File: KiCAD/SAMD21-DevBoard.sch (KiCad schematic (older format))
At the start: 23 parts, among them J1 .1\" Headers, J2 .1\" Headers, J3 Cortex_Debug, SW1 FSMCTTR, U1 SAMD21G18A-AU, Y1 32.768KHz

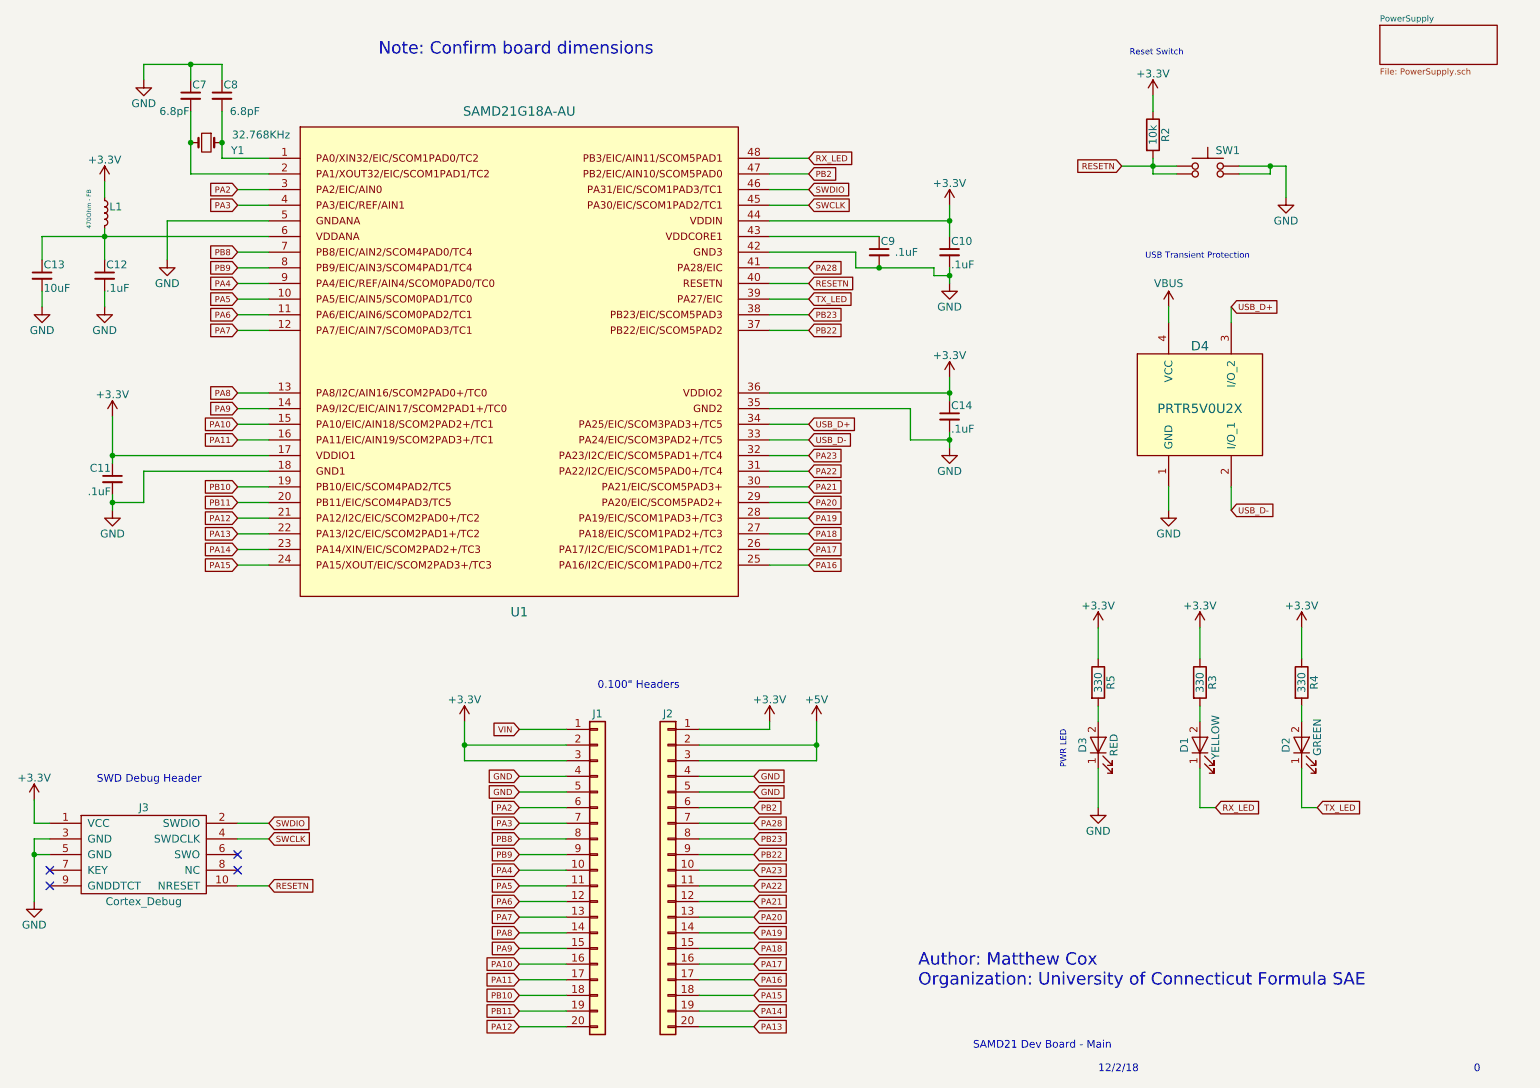
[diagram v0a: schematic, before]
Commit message: Fix library error
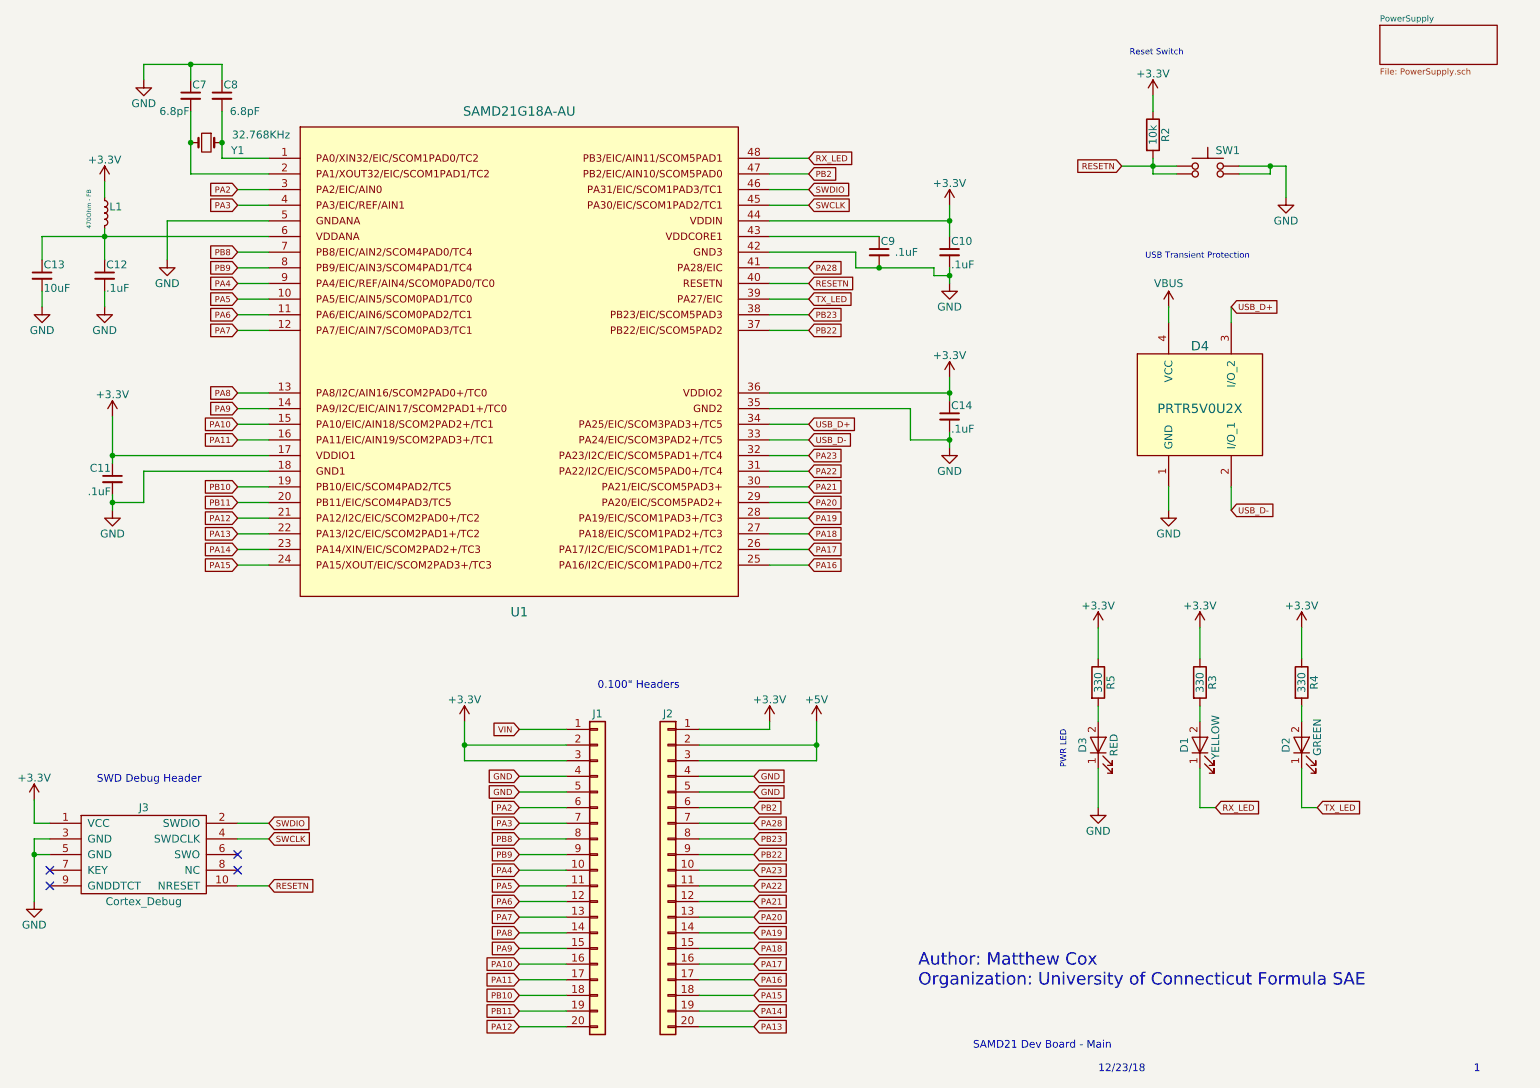
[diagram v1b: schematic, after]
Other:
- note added: "12/23/18"
- note added: "1\n"
- note removed: "0"
- note removed: "12/2/18"
- note removed: "Note: Confirm board dimensions"
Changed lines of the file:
@@
 EESchema Schematic File Version 2
+LIBS:SAMD21-DevBoard-rescue
 LIBS:power
 LIBS:device
@@
 SAMD21 Dev Board - Main
 Text Notes 8200 7650 0    49   ~ 0
-12/2/18
+12/23/18
 Text Notes 10600 7650 0    49   ~ 0
-0
+1\n
 Text Notes 7050 7100 0    79   ~ 0
 Author: Matthew Cox\nOrganization: University of Connecticut Formula SAE
@@
 	1    0    0    -1
 $EndComp
-Text Notes 3600 1150 0    79   ~ 0
-Note: Confirm board dimensions
 $Comp
 L FSMCTTR SW1

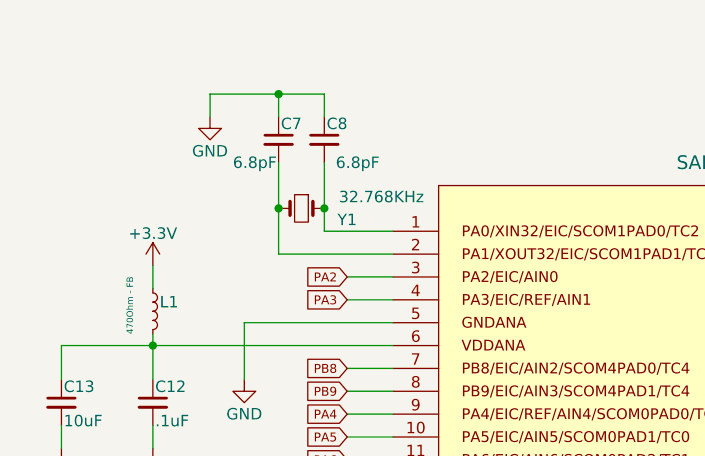
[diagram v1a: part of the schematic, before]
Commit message: Revised crystal symbol and updated layout slightly
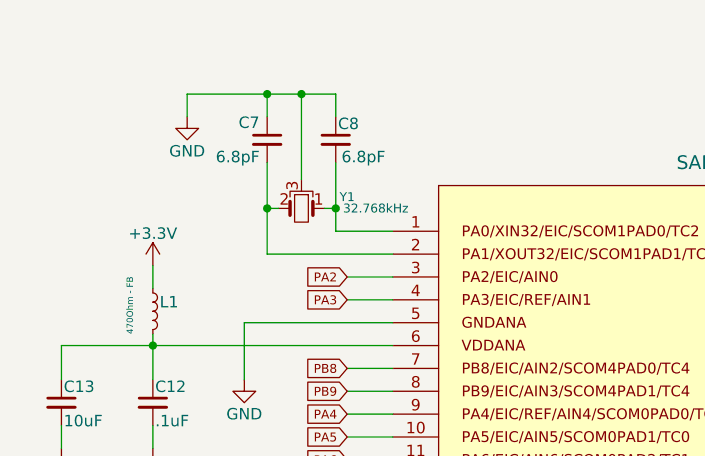
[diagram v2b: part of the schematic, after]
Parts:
- removed Y1: 32.768KHz, MS1V-T1K:MS1V-T1K, symbol Crystal_Small
- added Y1: 32.768kHz, MS1V-T1K:MS1V-T1K, symbol Crystal_GND3_Small
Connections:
- net GND: now also Y1.3
- net at C8.2, U1.1: now also Y1.1
- net at C7.2, U1.2: now also Y1.2
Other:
- moved on the sheet: C7, C8
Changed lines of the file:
@@
 USB_D+
-$Comp
-L Crystal_Small Y1
-U 1 1 5BF304E9
-P 2500 1700
-F 0 "Y1" H 2300 1750 50  0000 C CNN
-F 1 "32.768KHz" H 2150 1650 50  0000 C CNN
-F 2 "MS1V-T1K:MS1V-T1K" H 2500 1700 50  0001 C CNN
-F 3 "" H 2500 1700 50  0001 C CNN
-	1    2500 1700
-	-1   0    0    1
-$EndComp
 $Comp
 L C_Small C7
 U 1 1 5BF3056F
-P 2400 1400
-F 0 "C7" H 2410 1470 50  0000 L CNN
-F 1 "6.8pF" H 2200 1300 50  0000 L CNN
-F 2 "Capacitors_SMD:C_0805" H 2400 1400 50  0001 C CNN
-F 3 "" H 2400 1400 50  0001 C CNN
-	1    2400 1400
+P 2350 1400
+F 0 "C7" H 2225 1475 50  0000 L CNN
+F 1 "6.8pF" H 2125 1325 50  0000 L CNN
+F 2 "Capacitors_SMD:C_0805" H 2350 1400 50  0001 C CNN
+F 3 "" H 2350 1400 50  0001 C CNN
+	1    2350 1400
 	1    0    0    -1
 $EndComp
@@
 L C_Small C8
 U 1 1 5BF30598
-P 2600 1400
-F 0 "C8" H 2610 1470 50  0000 L CNN
-F 1 "6.8pF" H 2650 1300 50  0000 L CNN
-F 2 "Capacitors_SMD:C_0805" H 2600 1400 50  0001 C CNN
-F 3 "" H 2600 1400 50  0001 C CNN
-	1    2600 1400
+P 2650 1400
+F 0 "C8" H 2660 1470 50  0000 L CNN
+F 1 "6.8pF" H 2675 1325 50  0000 L CNN
+F 2 "Capacitors_SMD:C_0805" H 2650 1400 50  0001 C CNN
+F 3 "" H 2650 1400 50  0001 C CNN
+	1    2650 1400
 	1    0    0    -1
 $EndComp
@@
 L GND #PWR03
 U 1 1 5BF30CDB
-P 2100 1300
-F 0 "#PWR03" H 2100 1050 50  0001 C CNN
-F 1 "GND" H 2100 1150 50  0000 C CNN
-F 2 "" H 2100 1300 50  0001 C CNN
-F 3 "" H 2100 1300 50  0001 C CNN
-	1    2100 1300
+P 2000 1300
+F 0 "#PWR03" H 2000 1050 50  0001 C CNN
+F 1 "GND" H 2000 1150 50  0000 C CNN
+F 2 "" H 2000 1300 50  0001 C CNN
+F 3 "" H 2000 1300 50  0001 C CNN
+	1    2000 1300
 	1    0    0    -1
 $EndComp
@@
 	6100 3600 6350 3600
 Wire Wire Line
-	2600 1500 2600 1800
-Wire Wire Line
-	2600 1800 2900 1800
-Wire Wire Line
-	2400 1500 2400 1900
-Wire Wire Line
-	2400 1900 2900 1900
-Connection ~ 2400 1700
-Connection ~ 2600 1700
-Wire Wire Line
-	2600 1200 2600 1300
-Wire Wire Line
-	2100 1200 2600 1200
-Wire Wire Line
-	2400 1200 2400 1300
-Wire Wire Line
-	2100 1300 2100 1200
-Connection ~ 2400 1200
+	2000 1200 2650 1200
 Wire Wire Line
 	6100 2300 6800 2300
@@
 	1    0    0    -1
 $EndComp
+$Comp
+L Crystal_GND3_Small Y1
+U 1 1 5C436CC1
+P 2500 1700
+F 0 "Y1" H 2300 1650 39  0000 C CNN
+F 1 "32.768kHz" H 2175 1700 39  0000 C CNN
+F 2 "MS1V-T1K:MS1V-T1K" H 2500 1700 50  0001 C CNN
+F 3 "" H 2500 1700 50  0001 C CNN
+	1    2500 1700
+	-1   0    0    1
+$EndComp
+Wire Wire Line
+	2900 1800 2650 1800
+Wire Wire Line
+	2650 1800 2650 1500
+Wire Wire Line
+	2600 1700 2650 1700
+Connection ~ 2650 1700
+Wire Wire Line
+	2400 1700 2350 1700
+Wire Wire Line
+	2350 1500 2350 1900
+Wire Wire Line
+	2350 1900 2900 1900
+Connection ~ 2350 1700
+Wire Wire Line
+	2500 1575 2500 1200
+Connection ~ 2500 1200
+Wire Wire Line
+	2650 1200 2650 1300
+Wire Wire Line
+	2350 1300 2350 1200
+Connection ~ 2350 1200
+Wire Wire Line
+	2000 1300 2000 1200
 $EndSCHEMATC
